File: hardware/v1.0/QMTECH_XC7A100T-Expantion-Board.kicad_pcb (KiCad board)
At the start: 4 copper layers, 99.1 x 98.5 mm, 128 parts, among them J1 Micro_SD_Card_Det1, J10 Conn_01x06, J11 Conn_01x04, J12 Conn_01x34, J13 Conn_02x10_Odd_Even, J2 Conn_01x34, J3 USB_C_Receptacle_USB2.0_16P, J4 Conn_01x34, J5 Conn_01x03, J6 Conn_01x03, J7 Conn_01x04, J8 Conn_01x34, J9 Conn_01x34, U10 74LVC245A, U11 TLV62585, U12 CH32V003JxMx, U2 CH32V003JxMx, U3 AMS1117-1.8, U4 ADV7180BCP32Z-RL, U5 TLV62585, U6 74LVC245A, U7 TLV62585, U8 74LVC245A, U9 74LVC245A, Y1 28.63636MHz

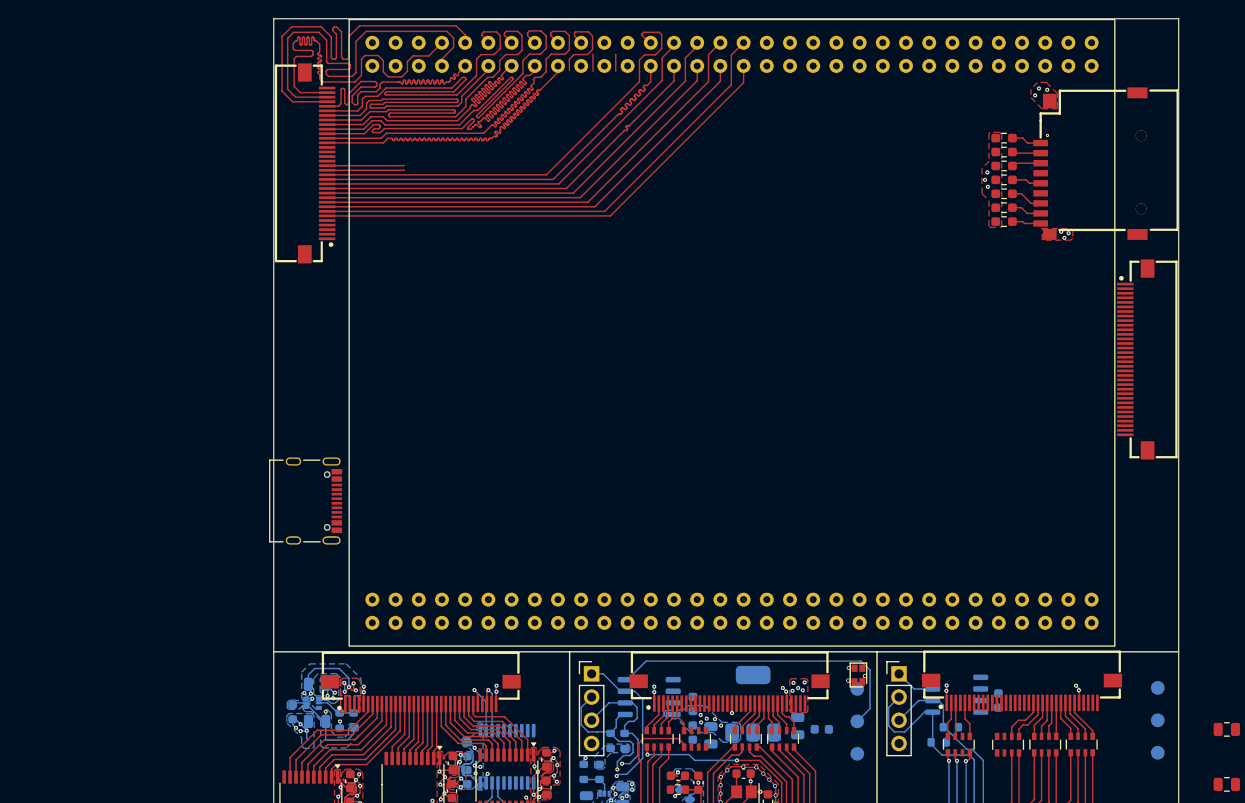
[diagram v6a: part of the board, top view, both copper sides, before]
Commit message: added pmod connectors instead of leds
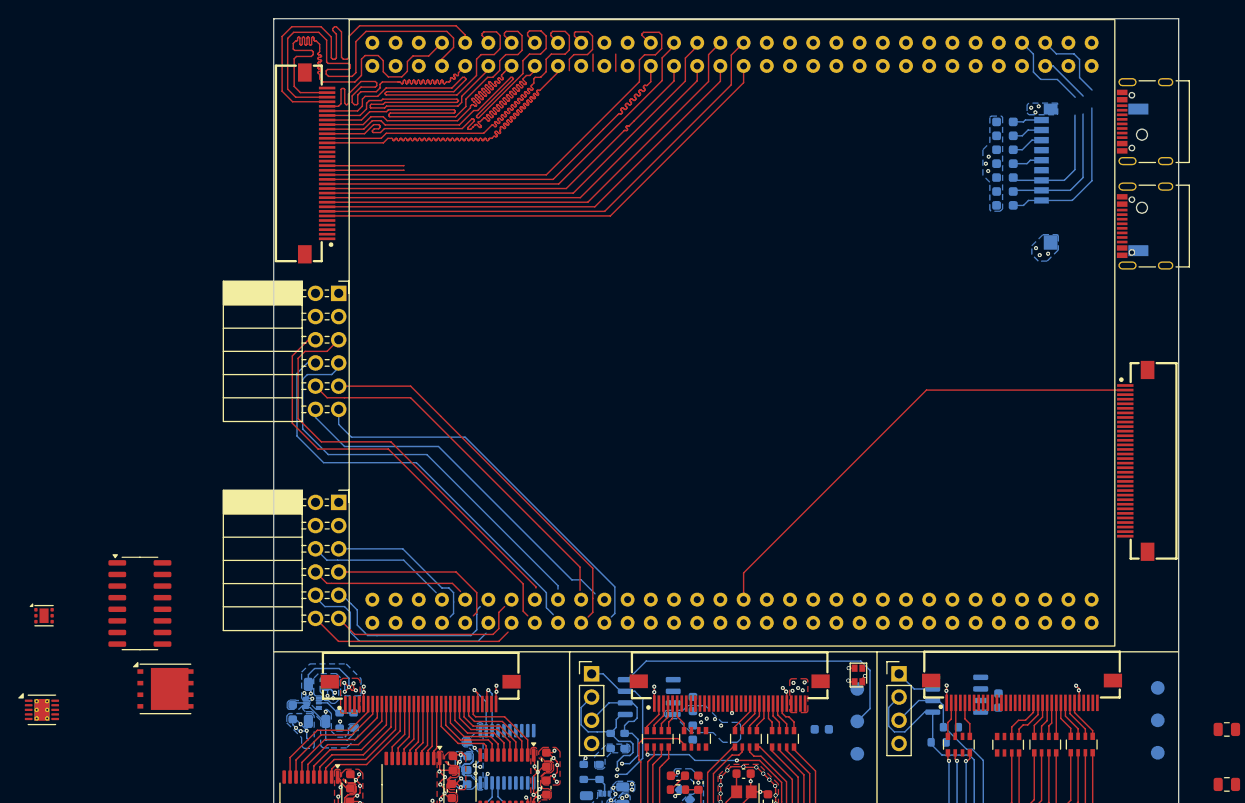
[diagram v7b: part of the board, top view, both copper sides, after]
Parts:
- removed C1, C9: 10uf, Capacitor_SMD:C_0805_2012Metric
- removed U3: AMS1117-1.8, Package_TO_SOT_SMD:SOT-223-3_TabPin2
- added J14: USB_C_Receptacle_USB2.0_16P, Connector_USB:USB_C_Receptacle_Palconn_UTC16-G, F.Cu at (156.4, 51.2)
- added J15: Conn_02x06_Top_Bottom, Connector_PinSocket_2.54mm:PinSocket_2x06_P2.54mm_Horizontal, F.Cu at (68.1, 70.0)
- added J16: Conn_02x06_Top_Bottom, Connector_PinSocket_2.54mm:PinSocket_2x06_P2.54mm_Horizontal, F.Cu at (68.1, 92.9)
- added Q1: AON6411, Package_DFN_QFN:AO_DFN-8-1EP_5.55x5.2mm_P1.27mm_EP4.12x4.6mm, F.Cu at (49.1, 113.3)
- added U13: TLV75718PDRV, Package_SON:WSON-6-1EP_2x2mm_P0.65mm_EP1x1.6mm, F.Cu at (35.8, 105.3)
- added U14: HUSB238, Package_DFN_QFN:DFN-10-1EP_3x3mm_P0.5mm_EP1.65x2.38mm_ThermalVias, F.Cu at (35.6, 115.6)
- added U15: CH340C, Package_SO:SOIC-16_3.9x9.9mm_P1.27mm, F.Cu at (46.3, 103.9)
- C4, C8: value 0.1uf -> 1uf
- J1: moved to B.Cu
- R1, R2, R3, R4, R5, R6, R7: value 4.7K -> 4.7k; moved to B.Cu
- R15, R20, R31: value 450K -> 450k
- R16, R21, R32: value 100K -> 100k
- R19: value 1K -> 1k
- R28, R29, R36, R37: value 4.7K -> 4.7k
- R8: value 10K -> 10k
- moved J3 95.8 mm to (156.4, 62.6), turned to 90 degrees
- moved J4 11.1 mm to (155.4, 88.3)
- moved R7 10.9 mm to (141.0, 51.2)
- moved R6 7.87 mm to (141.0, 52.7)
- moved R1 7.37 mm to (141.0, 60.4)
- moved R5 4.82 mm to (141.0, 54.3)
- moved R2 4.32 mm to (141.0, 58.8)
- moved J1 1.78 mm to (150.3, 57.6), turned to -90 degrees
- moved R4 1.78 mm to (141.0, 55.8)
- moved R3 1.28 mm to (141.0, 57.3)
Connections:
- J3 pad A5: /CC_MONIT1 -> /PD_CC1
- J3 pad A6: unconnected-(J3-D+-PadA6) -> /PD_D+
- J3 pad A7: unconnected-(J3-D--PadA7) -> /PD_D-
- J3 pad B5: /CC_MONIT2 -> /PD_CC2
- J3 pad B6: unconnected-(J3-D+-PadB6) -> /PD_D+
- J3 pad B7: unconnected-(J3-D--PadB7) -> /PD_D-
- U1 pad 100: unconnected-(U1B-IO_L2-Pad100) -> /PORT1_DE
- U1 pad 102: unconnected-(U1B-IO_K5-Pad102) -> /PORT1_BLUE0
- U1 pad 104: unconnected-(U1B-IO_L4-Pad104) -> /PORT1_BLUE2
- U1 pad 106: unconnected-(U1B-IO_N2-Pad106) -> /PORT1_BLUE4
- U1 pad 108: unconnected-(U1B-IO_M5_VREF-Pad108) -> /PORT1_BLUE6
- U1 pad 110: unconnected-(U1B-IO_J1-Pad110) -> /PORT1_GREEN0
- U1 pad 112: unconnected-(U1B-IO_P3-Pad112) -> /PORT1_GREEN2
- U1 pad 114: unconnected-(U1B-IO_T3-Pad114) -> /PORT1_GREEN4
- U1 pad 116: unconnected-(U1B-IO_P5_VREF-Pad116) -> /PORT1_GREEN6
- U1 pad 118: unconnected-(U1B-IO_M1-Pad118) -> /PORT1_RED0
- U1 pad 120: unconnected-(U1B-IO_P1-Pad120) -> /PORT1_RED2
- U1 pad 122: unconnected-(U1B-IO_R2-Pad122) -> /PORT1_RED4
- U1 pad 124: unconnected-(U1B-IO_U1-Pad124) -> /PORT1_RED6
- U1 pad 3: unconnected-(U1A-3V3-Pad3) -> +3V3
- U1 pad 4: unconnected-(U1A-3V3-Pad4) -> +3V3
- U1 pad 54: /SD_DAT2 -> /SD_DET
- U1 pad 55: /SD_DAT3 -> /SD_DAT1
- U1 pad 56: /SD_CMD -> /SD_DAT0
- U1 pad 58: /SD_DAT0 -> /SD_CMD
- U1 pad 59: /SD_DAT1 -> /SD_DAT3
- U1 pad 60: /SD_DET -> /SD_DAT2
- U1 pad 67: unconnected-(U1B-3V3-Pad67) -> +3V3
- U1 pad 68: unconnected-(U1B-3V3-Pad68) -> +3V3
- U1 pad 98: unconnected-(U1B-IO_G9_VREF-Pad98) -> /PORT1_CLK
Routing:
- net /PORT1_CLK: track 0.00 -> 53.0 mm
- net unconnected-(J15-Pin_6-Pad6): track 0.00 -> 46.9 mm
- net unconnected-(J15-Pin_8-Pad8): track 0.00 -> 46.5 mm
- net unconnected-(J15-Pin_7-Pad7): track 0.00 -> 45.9 mm
- net unconnected-(J15-Pin_5-Pad5): track 0.00 -> 45.7 mm
- net unconnected-(J15-Pin_11-Pad11): track 0.00 -> 42.7 mm
- net unconnected-(J15-Pin_9-Pad9): track 0.00 -> 41.6 mm
- net unconnected-(J15-Pin_10-Pad10): track 0.00 -> 39.7 mm
- net unconnected-(J15-Pin_12-Pad12): track 0.00 -> 39.5 mm
- net /SD_DAT2: track 3.32 -> 26.1 mm
- net unconnected-(J16-Pin_12-Pad12): track 0.00 -> 22.5 mm
- net unconnected-(J16-Pin_10-Pad10): track 0.00 -> 22.5 mm
- net unconnected-(J16-Pin_11-Pad11): track 0.00 -> 21.2 mm
- net unconnected-(J16-Pin_9-Pad9): track 0.00 -> 20.9 mm
- net /SD_CMD: track 3.22 -> 22.8 mm
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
